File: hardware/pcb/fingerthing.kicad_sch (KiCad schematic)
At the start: 46 parts, among them J1 10103594-0001LF, J2 TSW-118-07-L-D, J3 TSW-118-07-L-D, J4 SM03B-SRSS-TB(LF)(SN), SW1 434133025816, SW2 434133025816, U1 RP2350A, U2 NCP1117ST33T3G, U3 W25Q128JVSIQ, X1 12MHz

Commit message: usb / sensor layout
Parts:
- removed J1: 10103594-0001LF, RPI_COMPILED:amphenol_10103594-0001lf, symbol fingerthing:RP-019A1P-1JAX7V
- removed J2, J3: TSW-118-07-L-D, RPI_COMPILED:samtec_tsw-118-07-l-d, symbol fingerthing:RP-01JWH2-G371Y4
- removed PCB1: R4, symbol fingerthing:PCB_PWB_REV
- removed R4: 1k, RPI_COMPILED:generic_resc1005x35, symbol fingerthing:RP-019A1P-4Z6ZWY
- removed R9: 0, RPI_COMPILED:generic_resc1005x35, symbol fingerthing:RP-019A1P-4Y4V63
- removed SBREV1: S1, symbol fingerthing:SCH_BOM_REV
- removed SW2: 434133025816, RPI_COMPILED:wurthelek_434133025816, symbol fingerthing:RP-01H0MT-6E9H8F
- removed VARIANT1: RPI-RP2350A-MINIMAL, symbol fingerthing:VARIANT
- added D1: green, LED_SMD:LED_0603_1608Metric, symbol Device:LED
- added J1: USB4105-GF-A, Connector_USB:USB_C_Receptacle_GCT_USB4105-xx-A_16P_TopMnt_Horizontal, symbol Connector:USB_C_Receptacle_USB2.0_16P
- added J2: R503, Connector_JST:JST_SH_SM06B-SRSS-TB_1x06-1MP_P1.00mm_Horizontal, symbol Connector_Generic:Conn_01x06
- added R11, R12: 5.1k, Resistor_SMD:R_0402_1005Metric, symbol Device:R
- added R13: 1k, Resistor_SMD:R_0402_1005Metric, symbol Device:R
- added R14: 10k, Resistor_SMD:R_0402_1005Metric, symbol Device:R
- added SW3: 434133025816, RPI_COMPILED:wurthelek_434133025816, symbol fingerthing:RP-01H0MT-6E9H8F
- added U4: USBLC6-2SC6, Package_TO_SOT_SMD:SOT-23-6, symbol Power_Protection:USBLC6-2SC6
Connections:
- net +3V3: now also J2.1 (Pin_1), J2.6 (Pin_6), R14.1
- net GND: now also D1.1 (K), J1.A1 (GND), J1.A12 (GND), J1.B1 (GND), J1.B12 (GND), J1.SH (SHIELD), J2.2 (Pin_2), R11.2, R12.2, SW3.1, SW3.2, U4.2 (GND)
- net GPIO25: now also R13.1
- net GPIO4: now also J2.4 (Pin_4)
- net GPIO5: now also J2.3 (Pin_3)
- net GPIO6: now also R14.2, SW3.3, SW3.4
- net GPIO7: now also J2.5 (Pin_5)
- net USB_D+: now also J1.A6 (D+), J1.B6 (D+), U4.1 (I/O1), U4.6 (I/O1)
- net USB_D-: now also J1.A7 (D-), J1.B7 (D-), U4.3 (I/O2), U4.4 (I/O2)
- net VBUS: now also J1.A4 (VBUS), J1.A9 (VBUS), J1.B4 (VBUS), J1.B9 (VBUS), U4.5 (VBUS)
- net USB_DP: now reaches R7.2, U1.52 (USB_DP)
- net USB_DM: now reaches R8.2, U1.51 (USB_DM)
- net Net-(C4-Pad1): now reaches C4.1, R2.2, X1.3
- net GPIO0: no longer names the net of U1.2 (GPIO0)
- net GPIO1: no longer names the net of U1.3 (GPIO1)
- net GPIO10: no longer names the net of U1.14 (GPIO10)
- net GPIO11: no longer names the net of U1.15 (GPIO11)
- net GPIO12: no longer names the net of U1.16 (GPIO12)
- net GPIO13: no longer names the net of U1.17 (GPIO13)
- net GPIO14: no longer names the net of U1.18 (GPIO14)
- net GPIO15: no longer names the net of U1.19 (GPIO15)
- net GPIO16: no longer names the net of U1.27 (GPIO16)
- net GPIO17: no longer names the net of U1.28 (GPIO17)
- net GPIO18: no longer names the net of U1.29 (GPIO18)
- net GPIO19: no longer names the net of U1.31 (GPIO19)
- net GPIO2: no longer names the net of U1.4 (GPIO2)
- net GPIO20: no longer names the net of U1.32 (GPIO20)
- net GPIO21: no longer names the net of U1.33 (GPIO21)
- net GPIO22: no longer names the net of U1.34 (GPIO22)
- net GPIO23: no longer names the net of U1.35 (GPIO23)
- net GPIO24: no longer names the net of U1.36 (GPIO24)
- net GPIO26_ADC0: no longer names the net of U1.40 (GPIO26_ADC0)
- net GPIO27_ADC1: no longer names the net of U1.41 (GPIO27_ADC1)
- net GPIO28_ADC2: no longer names the net of U1.42 (GPIO28_ADC2)
- net GPIO29_ADC3: no longer names the net of U1.43 (GPIO29_ADC3)
- net GPIO3: no longer names the net of U1.5 (GPIO3)
- net GPIO8: no longer names the net of U1.12 (GPIO8)
- net GPIO9: no longer names the net of U1.13 (GPIO9)
- net RUN: no longer names the net of U1.26 (RUN)
- new net CC1: J1.A5 (CC1), R11.1
- new net CC2: J1.B5 (CC2), R12.1
- new net LED_A: D1.2 (A), R13.2
- no-connect marks 1 -> 28
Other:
- note added: "presence"
- note added: "sensor"
- note added: "status"
- note added: "usb"
- note removed: "12MHz Crystal"
- note removed: "BOOTSEL Button"
- note removed: "Flash"
- note removed: "IOs"
- note removed: "If using RP2354 (internal flash), remove R10. R9 can be fit to use U3 as secondary memory."
- note removed: "JST Debug Connector"
- note removed: "Make sure R7 and R8 are close to RP2350"
- note removed: "Note: S1 schematic revision indicates that this is the 1st revision of the schematic/BOM associated with the R4 PCB. R4-S1 therefore uniquely identifies the fully built PCB Assembly (PCBA). This is a change from the previous revision numbering to align with the internal Raspberry Pi product revisioning scheme"
- note removed: "Power"
- note removed: "RUN Button"
- moved on the sheet: C10, C11, C12, C13, C14, C15, C16, C17, C18, C8, J4

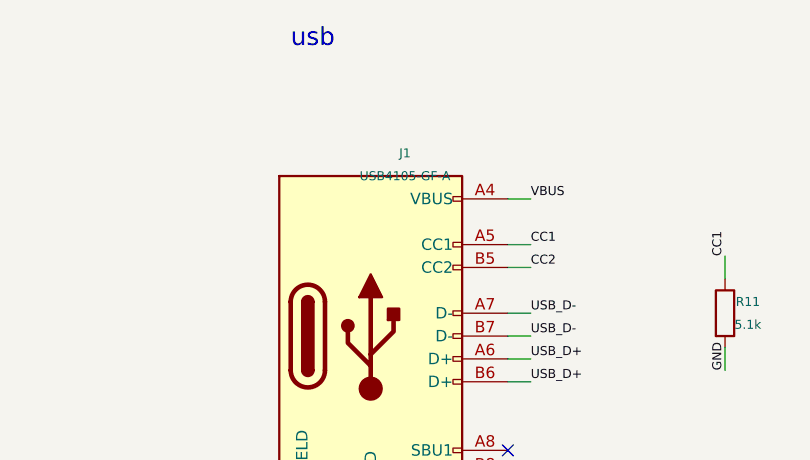
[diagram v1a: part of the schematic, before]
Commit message: pcb power / usb footprint
Ground and 3.3 V routing pass DRC clearance checks. ERC and schematic parity pass. 24 unconnected items remain.
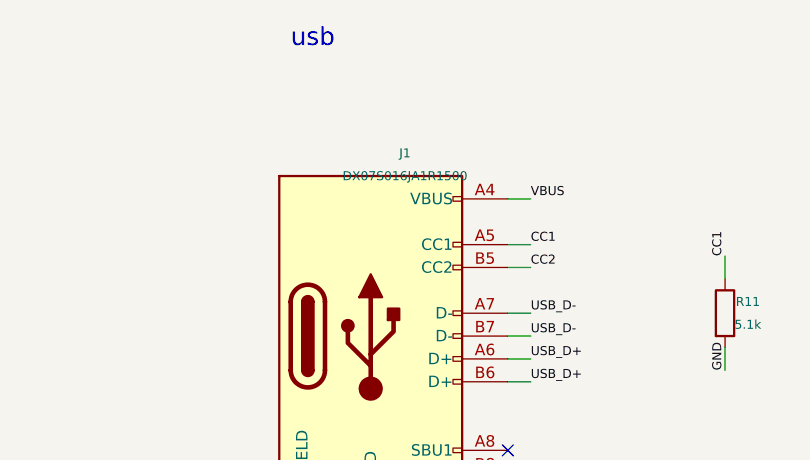
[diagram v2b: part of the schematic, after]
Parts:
- J1: value USB4105-GF-A -> DX07S016JA1R1500; footprint Connector_USB:USB_C_Receptacle_GCT_USB4105-xx-A_16P_TopMnt_Horizontal -> fingerthing:usb-c
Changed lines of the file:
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@@
 			)
 		)
-		(property "Value" "USB4105-GF-A"
+		(property "Value" "DX07S016JA1R1500"
 			(at 334.01 25.4 0)
 			(effects
@@
 			)
 		)
-		(property "Footprint" "Connector_USB:USB_C_Receptacle_GCT_USB4105-xx-A_16P_TopMnt_Horizontal"
+		(property "Footprint" "fingerthing:usb-c"
 			(at 330.2 43.18 0)
 			(effects

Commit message: esd bypass / sensor pinout
Added the USBLC6-2 VBUS bypass from the ST layout example. ERC, DRC and schematic parity pass with zero unconnected items. The R503 pinout follows GROW manual 2019.6 v1.1. Its MX1.0 plug needs a verified adapter cable for the board JST SH socket.
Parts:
- added C20: 100n, RPI_COMPILED:generic_capc1005x50, symbol fingerthing:RP-01BJ9Y-KRGF41
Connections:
- net GND: now also C20.2
- net VBUS: now also C20.1

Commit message: bom / usb power
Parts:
- D1: manufacturer (none) -> Lite-On; manufacturer_pn (none) -> LTST-C190KGKT
- J1: manufacturer (none) -> JAE; manufacturer_pn (none) -> DX07S016JA1R1500
- J2: manufacturer (none) -> JST; manufacturer_pn (none) -> SM06B-SRSS-TB(LF)(SN)
- R11, R12: manufacturer (none) -> Yageo; manufacturer_pn (none) -> RC0402FR-075K1L
- R13: manufacturer (none) -> Yageo; manufacturer_pn (none) -> RC0402FR-071KL
- R14: manufacturer (none) -> Yageo; manufacturer_pn (none) -> RC0402FR-0710KL
- SW3: manufacturer (none) -> Wurth Elektronik; manufacturer_pn (none) -> 434133025816
- U4: manufacturer (none) -> STMicroelectronics; manufacturer_pn (none) -> USBLC6-2SC6
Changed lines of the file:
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@@
 			)
 		)
-		(property "Datasheet" "https://www.usb.org/sites/default/files/documents/usb_type-c.zip"
+		(property "Datasheet" "https://www.mikrocontroller.net/attachment/650878/SJ121836.pdf"
 			(at 330.2 43.18 0)
 			(effects
@@
 					(unit 1)
 				)
+			)
+		)
+		(property "manufacturer" "JAE"
+			(at 334.01 25.4 0)
+			(hide yes)
+			(show_name no)
+			(do_not_autoplace no)
+			(effects
+				(font
+					(size 1.27 1.27)
+				)
+				(hide yes)
+			)
+		)
+		(property "manufacturer_pn" "DX07S016JA1R1500"
+			(at 334.01 25.4 0)
+			(hide yes)
+			(show_name no)
+			(do_not_autoplace no)
+			(effects
+				(font
+					(size 1.27 1.27)
+				)
+				(hide yes)
 			)
 		)
@@
 			)
 		)
-		(property "Datasheet" ""
+		(property "Datasheet" "https://yageogroup.com/component-documentation/download/specsheet/RC0402FR-075K1L"
 			(at 369.57 40.64 0)
 			(effects
@@
 					(unit 1)
 				)
+			)
+		)
+		(property "manufacturer" "Yageo"
+			(at 372.11 41.910000000000004 0)
+			(hide yes)
+			(show_name no)
+			(do_not_autoplace no)
+			(effects
+				(font
+					(size 1.27 1.27)
+				)
+				(hide yes)
+			)
+		)
+		(property "manufacturer_pn" "RC0402FR-075K1L"
+			(at 372.11 41.910000000000004 0)
+			(hide yes)
+			(show_name no)
+			(do_not_autoplace no)
+			(effects
+				(font
+					(size 1.27 1.27)
+				)
+				(hide yes)
 			)
 		)
@@
 			)
 		)
-		(property "Datasheet" ""
+		(property "Datasheet" "https://yageogroup.com/component-documentation/download/specsheet/RC0402FR-075K1L"
 			(at 389.89 40.64 0)
 			(effects
@@
 					(unit 1)
 				)
+			)
+		)
+		(property "manufacturer" "Yageo"
+			(at 392.43 41.910000000000004 0)
+			(hide yes)
+			(show_name no)
+			(do_not_autoplace no)
+			(effects
+				(font
+					(size 1.27 1.27)
+				)
+				(hide yes)
+			)
+		)
+		(property "manufacturer_pn" "RC0402FR-075K1L"
+			(at 392.43 41.910000000000004 0)
+			(hide yes)
+			(show_name no)
+			(do_not_autoplace no)
+			(effects
+				(font
+					(size 1.27 1.27)
+				)
+				(hide yes)
 			)
 		)
@@
 			)
 		)
+		(property "manufacturer" "STMicroelectronics"
+			(at 369.57 86.36 0)
+			(hide yes)
+			(show_name no)
+			(do_not_autoplace no)
+			(effects
+				(font
+					(size 1.27 1.27)
+				)
+				(hide yes)
+			)
+		)
+		(property "manufacturer_pn" "USBLC6-2SC6"
+			(at 369.57 86.36 0)
+			(hide yes)
+			(show_name no)
+			(do_not_autoplace no)
+			(effects
+				(font
+					(size 1.27 1.27)
+				)
+				(hide yes)
+			)
+		)
 	)
 	(symbol
@@
 			)
 		)
-		(property "Datasheet" ""
+		(property "Datasheet" "https://www.jst.com/products/crimp-style-connectors-wire-to-board-type/sh-connector"
 			(at 342.9 142.24 0)
 			(effects
@@
 					(unit 1)
 				)
+			)
+		)
+		(property "manufacturer" "JST"
+			(at 345.44 134.62 0)
+			(hide yes)
+			(show_name no)
+			(do_not_autoplace no)
+			(effects
+				(font
+					(size 1.27 1.27)
+				)
+				(hide yes)
+			)
+		)
+		(property "manufacturer_pn" "SM06B-SRSS-TB(LF)(SN)"
+			(at 345.44 134.62 0)
+			(hide yes)
+			(show_name no)
+			(do_not_autoplace no)
+			(effects
+				(font
+					(size 1.27 1.27)
+				)
+				(hide yes)
 			)
 		)
@@
 			)
 		)
-		(property "Datasheet" "file:///C:\\rpi-pdb\\parts\\Electromechanical\\Switches\\Tactile\\WURTHELEK_434133025816\\datasheets"
+		(property "Datasheet" "https://www.we-online.com/components/products/datasheet/434133025816.pdf"
 			(at 330.2 177.8 0)
 			(effects
@@
 					(unit 1)
 				)
+			)
+		)
+		(property "manufacturer" "Wurth Elektronik"
+			(at 330.2 175.26000000000002 0)
+			(hide yes)
+			(show_name no)
+			(do_not_autoplace no)
+			(effects
+				(font
+					(size 1.27 1.27)
+				)
+				(hide yes)
+			)
+		)
+		(property "manufacturer_pn" "434133025816"
+			(at 330.2 175.26000000000002 0)
+			(hide yes)
+			(show_name no)
+			(do_not_autoplace no)
+			(effects
+				(font
+					(size 1.27 1.27)
+				)
+				(hide yes)
 			)
 		)
@@
 			)
 		)
-		(property "Datasheet" ""
+		(property "Datasheet" "https://yageogroup.com/component-documentation/download/specsheet/RC0402FR-0710KL"
 			(at 365.76 175.26 0)
 			(effects
@@
 					(unit 1)
 				)
+			)
+		)
+		(property "manufacturer" "Yageo"
+			(at 368.3 176.53 0)
+			(hide yes)
+			(show_name no)
+			(do_not_autoplace no)
+			(effects
+				(font
+					(size 1.27 1.27)
+				)
+				(hide yes)
+			)
+		)
+		(property "manufacturer_pn" "RC0402FR-0710KL"
+			(at 368.3 176.53 0)
+			(hide yes)
+			(show_name no)
+			(do_not_autoplace no)
+			(effects
+				(font
+					(size 1.27 1.27)
+				)
+				(hide yes)
 			)
 		)
@@
 			)
 		)
-		(property "Datasheet" ""
+		(property "Datasheet" "https://optoelectronics.liteon.com/upload/download/DS22-2000-074/LTST-C190KGKT.PDF"
 			(at 365.76 210.82 0)
 			(effects
@@
 					(unit 1)
 				)
+			)
+		)
+		(property "manufacturer" "Lite-On"
+			(at 365.76 208.28 0)
+			(hide yes)
+			(show_name no)
+			(do_not_autoplace no)
+			(effects
+				(font
+					(size 1.27 1.27)
+				)
+				(hide yes)
+			)
+		)
+		(property "manufacturer_pn" "LTST-C190KGKT"
+			(at 365.76 208.28 0)
+			(hide yes)
+			(show_name no)
+			(do_not_autoplace no)
+			(effects
+				(font
+					(size 1.27 1.27)
+				)
+				(hide yes)
 			)
 		)
@@
 			)
 		)
-		(property "Datasheet" ""
+		(property "Datasheet" "https://yageogroup.com/component-documentation/download/specsheet/RC0402FR-071KL"
 			(at 389.89 203.2 0)
 			(effects
@@
 			)
 		)
+		(property "manufacturer" "Yageo"
+			(at 392.43 204.47 0)
+			(hide yes)
+			(show_name no)
+			(do_not_autoplace no)
+			(effects
+				(font
+					(size 1.27 1.27)
+				)
+				(hide yes)
+			)
+		)
+		(property "manufacturer_pn" "RC0402FR-071KL"
+			(at 392.43 204.47 0)
+			(hide yes)
+			(show_name no)
+			(do_not_autoplace no)
+			(effects
+				(font
+					(size 1.27 1.27)
+				)
+				(hide yes)
+			)
+		)

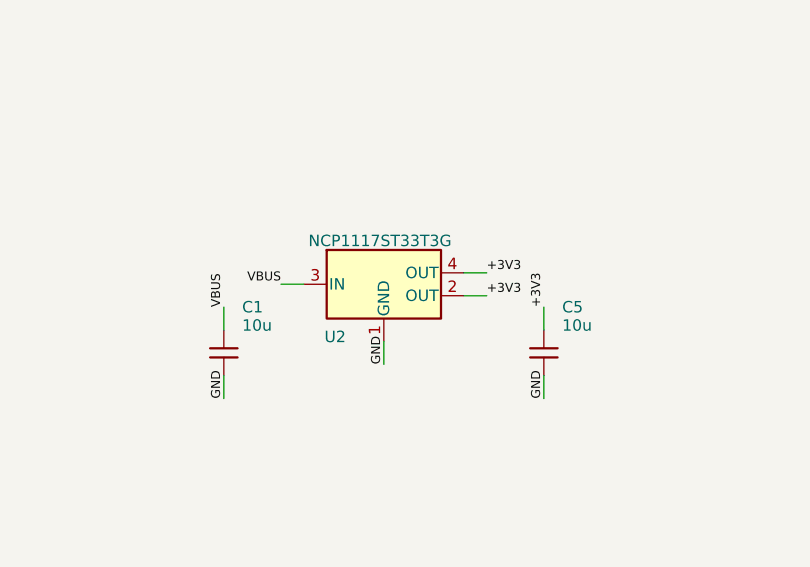
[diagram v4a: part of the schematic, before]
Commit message: 3v3 regulator / capacitor routing
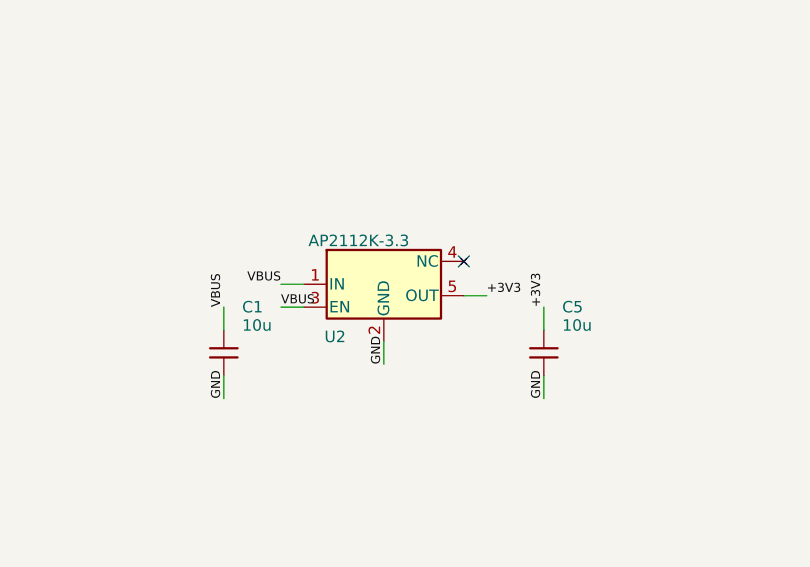
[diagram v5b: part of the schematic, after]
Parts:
- U2: value NCP1117ST33T3G -> AP2112K-3.3; footprint RPI_COMPILED:onsemi_ncp1117st33t3g -> Package_TO_SOT_SMD:SOT-23-5; symbol fingerthing:RP-01JWD9-7JRX6J -> fingerthing:AP2112K-3.3; current 1A -> (none); manufacturer ON Semiconductor -> Diodes Incorporated; manufacturer_pn NCP1117ST33T3G -> AP2112K-3.3TRG1; operating_temp_max +125C -> (none); operating_temp_min +0C -> (none); package SOT-223 -> (none); packaging Tape & Reel -> (none); packaging_qty 4000 -> (none); part_uid RP-01JWD9-7JRX6J -> (none); size 6.5x7x1.8mm -> (none); voltage 3.3V -> (none); z_height_max 1.8mm -> (none); z_height_nom 1.8mm -> (none)
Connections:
- net +3V3: now also U2.5 (OUT); no longer U2.2 (OUT), U2.4 (OUT)
- net GND: now also U2.2 (GND); no longer U2.1 (GND)
- net VBUS: now also U2.1 (IN)
- no-connect marks 28 -> 29
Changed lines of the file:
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@@
 	)
 	(symbol
-		(lib_id "fingerthing:RP-01JWD9-7JRX6J")
+		(lib_id "fingerthing:AP2112K-3.3")
 		(at 76.2 44.45 0)
 		(unit 1)
@@
 			)
 		)
-		(property "Value" "NCP1117ST33T3G"
+		(property "Value" "AP2112K-3.3"
 			(at 67.818 39.624 0)
 			(show_name no)
@@
 			)
 		)
-		(property "Footprint" "RPI_COMPILED:onsemi_ncp1117st33t3g"
+		(property "Footprint" "Package_TO_SOT_SMD:SOT-23-5"
 			(at 76.2 36.195 0)
 			(hide yes)
@@
 			)
 		)
-		(property "Datasheet" "file:///C:\\rpi-pdb\\parts\\Integrated_Circuits\\Power\\LDO\\ONSEMI_NCP1117ST33T3G\\datasheets"
+		(property "Datasheet" "https://www.diodes.com/assets/Datasheets/AP2112.pdf"
 			(at 76.2 41.91 0)
 			(hide yes)
@@
 			)
 		)
-		(property "Description" "LDO, Vin=4.75-20V, Vout=3.3V, 1A min, SOT-223"
+		(property "Description" "3.3 V LDO with enable, SOT25"
 			(at 76.2 44.45 0)
 			(hide yes)
@@
 			)
 		)
-		(property "part_uid" "RP-01JWD9-7JRX6J"
+		(property "manufacturer" "Diodes Incorporated"
 			(at 76.2 44.45 0)
 			(hide yes)
@@
 			)
 		)
-		(property "manufacturer" "ON Semiconductor"
+		(property "manufacturer_pn" "AP2112K-3.3TRG1"
 			(at 76.2 44.45 0)
 			(hide yes)
@@
 			)
 		)
-		(property "manufacturer_pn" "NCP1117ST33T3G"
-			(at 76.2 44.45 0)
-			(hide yes)
-			(show_name no)
-			(do_not_autoplace no)
-			(effects
-				(font
-					(size 1.27 1.27)
-				)
-				(hide yes)
-			)
-		)
-		(property "packaging" "Tape & Reel"
-			(at 76.2 44.45 0)
-			(hide yes)
-			(show_name no)
-			(do_not_autoplace no)
-			(effects
-				(font
-					(size 1.27 1.27)
-				)
-				(hide yes)
-			)
-		)
-		(property "packaging_qty" "4000"
-			(at 76.2 44.45 0)
-			(hide yes)
-			(show_name no)
-			(do_not_autoplace no)
-			(effects
-				(font
-					(size 1.27 1.27)
-				)
-				(hide yes)
-			)
-		)
-		(property "voltage" "3.3V"
-			(at 76.2 44.45 0)
-			(hide yes)
-			(show_name no)
-			(do_not_autoplace no)
-			(effects
-				(font
-					(size 1.27 1.27)
-				)
-				(hide yes)
-			)
-		)
-		(property "operating_temp_max" "+125C"
-			(at 76.2 44.45 0)
-			(hide yes)
-			(show_name no)
-			(do_not_autoplace no)
-			(effects
-				(font
-					(size 1.27 1.27)
-				)
-				(hide yes)
-			)
-		)
-		(property "operating_temp_min" "+0C"
-			(at 76.2 44.45 0)
-			(hide yes)
-			(show_name no)
-			(do_not_autoplace no)
-			(effects
-				(font
-					(size 1.27 1.27)
-				)
-				(hide yes)
-			)
-		)
-		(property "z_height_max" "1.8mm"
-			(at 76.2 44.45 0)
-			(hide yes)
-			(show_name no)
-			(do_not_autoplace no)
-			(effects
-				(font
-					(size 1.27 1.27)
-				)
-				(hide yes)
-			)
-		)
-		(property "package" "SOT-223"
-			(at 76.2 44.45 0)
-			(hide yes)
-			(show_name no)
-			(do_not_autoplace no)
-			(effects
-				(font
-					(size 1.27 1.27)
-				)
-				(hide yes)
-			)
-		)
-		(property "size" "6.5x7x1.8mm"
-			(at 76.2 44.45 0)
-			(hide yes)
-			(show_name no)
-			(do_not_autoplace no)
-			(effects
-				(font
-					(size 1.27 1.27)
-				)
-				(hide yes)
-			)
-		)
-		(property "current" "1A"
-			(at 76.2 44.45 0)
-			(hide yes)
-			(show_name no)
-			(do_not_autoplace no)
-			(effects
-				(font
-					(size 1.27 1.27)
-				)
-				(hide yes)
-			)
-		)
-		(property "z_height_nom" "1.8mm"
-			(at 76.2 44.45 0)
-			(hide yes)
-			(show_name no)
-			(do_not_autoplace no)
-			(effects
-				(font
-					(size 1.27 1.27)
+		(instances
+			(project "fingerthing"
+				(path "/94683f5c-9cd9-448e-be96-9792537b5cb8"
+					(reference "U2")
+					(unit 1)
 				)
-				(hide yes)
 			)
 		)
@@
 		(pin "4"
 		)
-		(instances
-			(project "fingerthing"
-				(path "/94683f5c-9cd9-448e-be96-9792537b5cb8"
-					(reference "U2")
-					(unit 1)
-				)
-			)
+		(pin "5"
 		)
 	)
@@
 	(wire
 		(pts
-			(xy 85.09 43.18)
-			(xy 87.63 43.18)
-		)
-		(stroke
-			(width 0)
-			(type default)
-		)
-	)
-	(label "+3V3"
-		(at 87.63 43.18 0)
-		(effects
-			(font
-				(size 1.0 1.0)
-			)
-			(justify left bottom)
-		)
-	)
-	(wire
-		(pts
 			(xy 58.42 49.53)
 			(xy 58.42 46.99)
@@
 		)
 	)
+	(wire
+		(pts
+			(xy 67.31 46.99)
+			(xy 64.77 46.99)
+		)
+		(stroke
+			(width 0)
+			(type default)
+		)
+	)
+	(label "VBUS"
+		(at 64.77 46.99 0)
+		(effects
+			(font
+				(size 1.0 1.0)
+			)
+			(justify left bottom)
+		)
+	)
+	(no_connect
+		(at 85.09 41.91)
+	)
 )

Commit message: sensor switch / pcb
TPS22919DCKR switches both R503 supplies from GP8. Added input and output bypass, ON pull-down and switched RX pull-up. The QOD pin uses a passive symbol type for its connection to OUT. ERC, DRC and schematic parity pass with zero unconnected items. Firmware control and physical power checks remain.
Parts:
- added C21: 1u, Capacitor_SMD:C_0402_1005Metric, symbol fingerthing:RP-01BJ9Y-KRGF41
- added C22: 100n, RPI_COMPILED:generic_capc1005x50, symbol fingerthing:RP-01BJ9Y-KRGF41
- added R15: 100k, Resistor_SMD:R_0402_1005Metric, symbol Device:R
- added R16: 10k, Resistor_SMD:R_0402_1005Metric, symbol Device:R
- added U5: TPS22919DCK, Package_TO_SOT_SMD:SOT-363_SC-70-6, symbol fingerthing:TPS22919DCK
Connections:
- net +3V3: now also C21.1, U5.1 (IN); no longer J2.1 (Pin_1), J2.6 (Pin_6)
- net GND: now also C21.2, C22.2, R15.2, U5.2 (GND)
- net GPIO4: now also R16.2
- net GPIO8: now reaches U1.12 (GPIO8)
- net GPIO8: now also R15.1, U5.3 (ON)
- new net SENSOR_3V3: C22.1, J2.1 (Pin_1), J2.6 (Pin_6), R16.1, U5.5 (QOD), U5.6 (OUT)
